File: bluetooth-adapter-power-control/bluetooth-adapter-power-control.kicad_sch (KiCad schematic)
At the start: 0 parts

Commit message: bluetooth-adapter-power-control: Finish schematic
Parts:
- added C1: 100n, symbol Device:C_Small
- added D1, D2: RED, symbol Device:LED
- added J1: UPDI, symbol Connector:Conn_01x03_Socket
- added J2: HDR, symbol Connector:Conn_01x05_Socket
- added Q1: NMOS, symbol Simulation_SPICE:NMOS
- added R1, R4: 10k, symbol Device:R
- added R2: 7.5k, symbol Device:R
- added R3, R5, R6: 1k, symbol Device:R
- added TP1: TestPoint, symbol Connector:TestPoint
- added U1: ATtiny202-SSNR, Package_SO:SOIC-8_3.9x4.9mm_P1.27mm, symbol MCU_Microchip_ATtiny:ATtiny202-SS
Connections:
- new net: Q1.2 (G), R3.2, R4.1
- new net: TP1.1, U1.2 (PA6)
- new net: R6.1, U1.3 (PA7)
- new net: D2.2 (A), R6.2
- new net: D1.2 (A), R5.2
- new net +5V: C1.1, J1.1 (Pin_1), J2.1 (Pin_1), R5.1, U1.1 (VCC)
- new net BTN1: Q1.1 (D)
- new net BTN2: Q1.3 (S)
- new net BTN_SHORT: J2.4 (Pin_4), R3.1, U1.5 (PA2)
- new net BT_LED_IN: J2.5 (Pin_5), U1.7 (PA3)
- new net CAR_ON: J2.3 (Pin_3), R1.2, R2.1, U1.4 (PA1)
- new net GND: C1.2, D1.1 (K), D2.1 (K), J1.3 (Pin_3), J2.2 (Pin_2), R2.2, R4.2, U1.8 (GND)
- new net IGNITION_IN: R1.1
- new net UPDI: J1.2 (Pin_2), U1.6 (~{RESET}/PA0)

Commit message: bluetooth-adapter-power-control: add footprints
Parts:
- C1: footprint (none) -> Capacitor_SMD:C_0603_1608Metric
- D1, D2: footprint (none) -> LED_SMD:LED_0603_1608Metric
- J1: footprint (none) -> Connector_PinHeader_1.27mm:PinHeader_1x05_P1.27mm_Vertical
- J2: footprint (none) -> Connector_PinHeader_1.27mm:PinHeader_1x03_P1.27mm_Vertical
- Q1: footprint (none) -> Package_TO_SOT_SMD:SOT-23
- R1, R2, R3, R4, R5, R6: footprint (none) -> Resistor_SMD:R_0603_1608Metric
- TP1: footprint (none) -> TestPoint:TestPoint_Pad_D1.0mm
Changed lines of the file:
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@@
 			)
 		)
-		(property "Footprint" ""
+		(property "Footprint" "Package_TO_SOT_SMD:SOT-23"
 			(at 60.96 101.6 0)
 			(effects
@@
 			)
 		)
-		(property "Footprint" ""
+		(property "Footprint" "Connector_PinHeader_1.27mm:PinHeader_1x05_P1.27mm_Vertical"
 			(at 50.8 149.86 0)
 			(effects
@@
 			)
 		)
-		(property "Footprint" ""
+		(property "Footprint" "TestPoint:TestPoint_Pad_D1.0mm"
 			(at 156.21 107.95 0)
 			(effects
@@
 			)
 		)
-		(property "Footprint" ""
+		(property "Footprint" "Resistor_SMD:R_0603_1608Metric"
 			(at 154.432 111.76 90)
 			(effects
@@
 			)
 		)
-		(property "Footprint" ""
+		(property "Footprint" "LED_SMD:LED_0603_1608Metric"
 			(at 193.04 106.68 0)
 			(effects
@@
 			)
 		)
-		(property "Footprint" ""
+		(property "Footprint" "Resistor_SMD:R_0603_1608Metric"
 			(at 38.862 110.49 90)
 			(effects
@@
 			)
 		)
-		(property "Footprint" ""
+		(property "Footprint" "Resistor_SMD:R_0603_1608Metric"
 			(at 38.862 97.79 90)
 			(effects
@@
 			)
 		)
-		(property "Footprint" ""
+		(property "Footprint" "Connector_PinHeader_1.27mm:PinHeader_1x03_P1.27mm_Vertical"
 			(at 250.19 105.41 0)
 			(effects
@@
 			)
 		)
-		(property "Footprint" ""
+		(property "Footprint" "LED_SMD:LED_0603_1608Metric"
 			(at 156.21 121.92 0)
 			(effects
@@
 			)
 		)
-		(property "Footprint" ""
+		(property "Footprint" "Resistor_SMD:R_0603_1608Metric"
 			(at 40.132 59.69 90)
 			(effects
@@
 			)
 		)
-		(property "Footprint" ""
+		(property "Footprint" "Resistor_SMD:R_0603_1608Metric"
 			(at 191.262 96.52 90)
 			(effects
@@
 			)
 		)
-		(property "Footprint" ""
+		(property "Footprint" "Resistor_SMD:R_0603_1608Metric"
 			(at 40.132 49.53 90)
 			(effects
@@
 			)
 		)
-		(property "Footprint" ""
+		(property "Footprint" "Capacitor_SMD:C_0603_1608Metric"
 			(at 93.98 100.33 0)
 			(effects

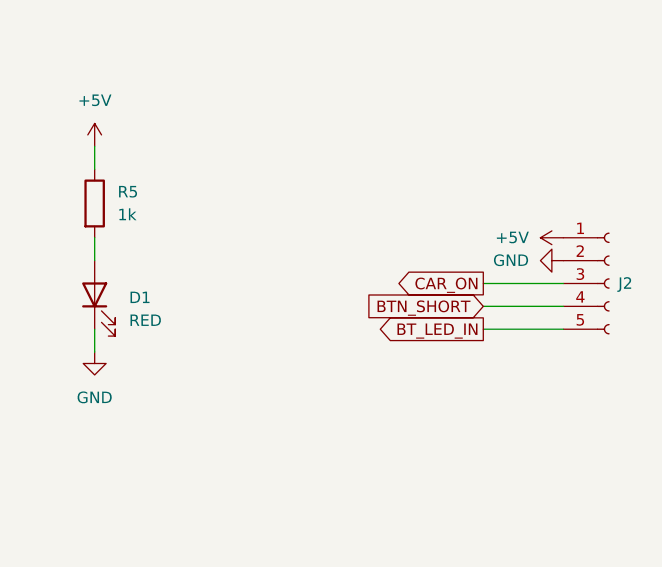
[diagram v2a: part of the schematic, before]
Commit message: bluetooth-adapter-power-control: Fix schematic & footprints, update PCB
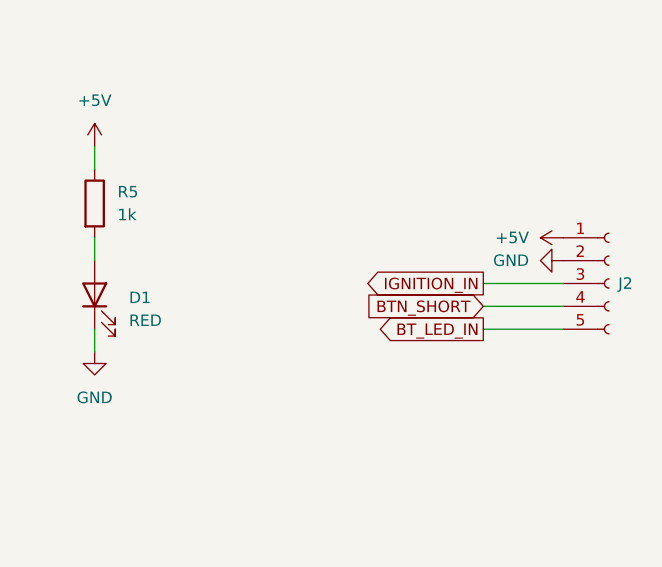
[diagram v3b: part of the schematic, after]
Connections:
- net CAR_ON: no longer J2.3 (Pin_3)
- net IGNITION_IN: now also J2.3 (Pin_3)
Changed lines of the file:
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@@
-		)
-	)
-	(global_label "CAR_ON"
-		(shape output)
-		(at 236.22 105.41 180)
-		(fields_autoplaced yes)
-		(effects
-			(font
-				(size 1.27 1.27)
-			)
-			(justify right)
-		)
-		(property "Intersheetrefs" "${INTERSHEET_REFS}"
-			(at 225.9776 105.41 0)
-			(effects
-				(font
-					(size 1.27 1.27)
-				)
-				(justify right)
-				(hide yes)
-			)
 		)
 	)
@@
 				(hide yes)
 			)
+		)
+	)
+	(global_label "IGNITION_IN"
+		(shape output)
+		(at 236.22 105.41 180)
+		(fields_autoplaced yes)
+		(effects
+			(font
+				(size 1.27 1.27)
+			)
+			(justify right)
+		)
+		(property "Intersheetrefs" "${INTERSHEET_REFS}"
+			(at 222.2884 105.41 0)
+			(effects
+				(font
+					(size 1.27 1.27)
+				)
+				(justify right)
+				(hide yes)
+			)

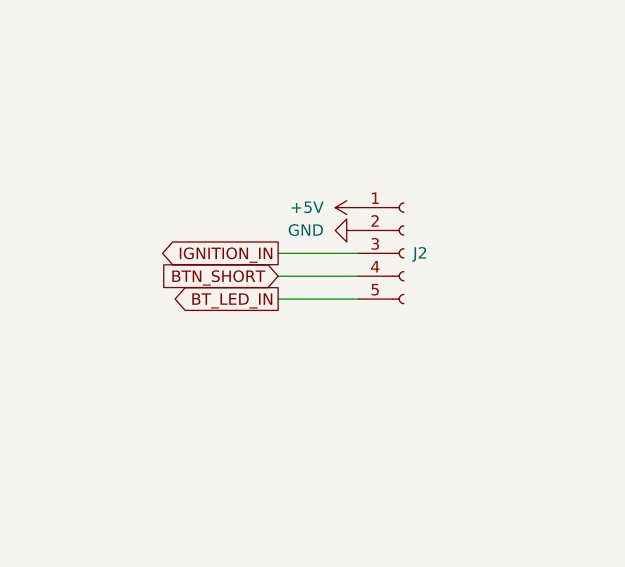
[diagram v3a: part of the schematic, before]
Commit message: bluetooth-adapter-power-control: change 5 pin header to 7 to include button short pins
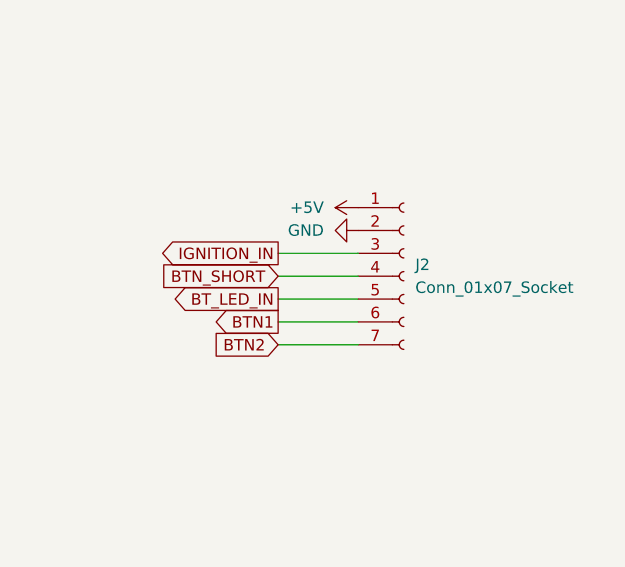
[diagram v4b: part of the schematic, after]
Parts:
- removed J2: HDR, Connector_PinHeader_1.27mm:PinHeader_1x03_P1.27mm_Vertical, symbol Connector:Conn_01x05_Socket
- added J2: Conn_01x07_Socket, Connector_PinHeader_1.27mm:PinHeader_1x07_P1.27mm_Vertical, symbol Connector:Conn_01x07_Socket
- J1: footprint Connector_PinHeader_1.27mm:PinHeader_1x05_P1.27mm_Vertical -> Connector_PinHeader_1.27mm:PinHeader_1x03_P1.27mm_Vertical
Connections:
- net +5V: now also J2.1 (Pin_1)
- net BTN1: now also J2.6 (Pin_6)
- net BTN2: now also J2.7 (Pin_7)
- net BTN_SHORT: now also J2.4 (Pin_4)
- net BT_LED_IN: now also J2.5 (Pin_5)
- net GND: now also J2.2 (Pin_2)
- net IGNITION_IN: now also J2.3 (Pin_3)
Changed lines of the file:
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@@
+	(wire
+		(pts
+			(xy 236.22 115.57) (xy 245.11 115.57)
+		)
+		(stroke
+			(width 0)
+			(type default)
+		)
+	)
+	(wire
+		(pts
+			(xy 236.22 113.03) (xy 245.11 113.03)
+		)
+		(stroke
+			(width 0)
+			(type default)
+		)
+	)
 	(wire
 		(pts
@@
 		)
 	)
+	(global_label "BTN2"
+		(shape input)
+		(at 236.22 115.57 180)
+		(fields_autoplaced yes)
+		(effects
+			(font
+				(size 1.27 1.27)
+			)
+			(justify right)
+		)
+		(property "Intersheetrefs" "${INTERSHEET_REFS}"
+			(at 228.4572 115.57 0)
+			(effects
+				(font
+					(size 1.27 1.27)
+				)
+				(justify right)
+				(hide yes)
+			)
+		)
+	)
 	(global_label "CAR_ON"
 		(shape input)
@@
 		(property "Intersheetrefs" "${INTERSHEET_REFS}"
 			(at 222.2884 105.41 0)
+			(effects
+				(font
+					(size 1.27 1.27)
+				)
+				(justify right)
+				(hide yes)
+			)
+		)
+	)
+	(global_label "BTN1"
+		(shape output)
+		(at 236.22 113.03 180)
+		(fields_autoplaced yes)
+		(effects
+			(font
+				(size 1.27 1.27)
+			)
+			(justify right)
+		)
+		(property "Intersheetrefs" "${INTERSHEET_REFS}"
+			(at 228.4572 113.03 0)
 			(effects
 				(font
@@
 			)
 		)
-		(property "Footprint" "Connector_PinHeader_1.27mm:PinHeader_1x05_P1.27mm_Vertical"
+		(property "Footprint" "Connector_PinHeader_1.27mm:PinHeader_1x03_P1.27mm_Vertical"
 			(at 50.8 149.86 0)
 			(effects
@@
 				(path "/cb952256-1cf9-427a-8657-67ac3ee7eb3e"
 					(reference "J1")
+					(unit 1)
+				)
+			)
+		)
+	)
+	(symbol
+		(lib_id "Connector:Conn_01x07_Socket")
+		(at 250.19 107.95 0)
+		(unit 1)
+		(exclude_from_sim no)
+		(in_bom yes)
+		(on_board yes)
+		(dnp no)
+		(fields_autoplaced yes)
+		(property "Reference" "J2"
+			(at 251.46 106.6799 0)
+			(effects
+				(font
+					(size 1.27 1.27)
+				)
+				(justify left)
+			)
+		)
+		(property "Value" "Conn_01x07_Socket"
+			(at 251.46 109.2199 0)
+			(effects
+				(font
+					(size 1.27 1.27)
+				)
+				(justify left)
+			)
+		)
+		(property "Footprint" "Connector_PinHeader_1.27mm:PinHeader_1x07_P1.27mm_Vertical"
+			(at 250.19 107.95 0)
+			(effects
+				(font
+					(size 1.27 1.27)
+				)
+				(hide yes)
+			)
+		)
+		(property "Datasheet" "~"
+			(at 250.19 107.95 0)
+			(effects
+				(font
+					(size 1.27 1.27)
+				)
+				(hide yes)
+			)
+		)
+		(property "Description" "Generic connector, single row, 01x07, script generated"
+			(at 250.19 107.95 0)
+			(effects
+				(font
+					(size 1.27 1.27)
+				)
+				(hide yes)
+			)
+		)
+		(pin "1"
+		)
+		(pin "6"
+		)
+		(pin "5"
+		)
+		(pin "2"
+		)
+		(pin "3"
+		)
+		(pin "4"
+		)
+		(pin "7"
+		)
+		(instances
+			(project ""
+				(path "/cb952256-1cf9-427a-8657-67ac3ee7eb3e"
+					(reference "J2")
 					(unit 1)
 				)
@@
 					(unit 1)
 				)
-			)
-		)
-	)
-	(symbol
-		(lib_id "Connector:Conn_01x05_Socket")
-		(at 250.19 105.41 0)
-		(unit 1)
-		(exclude_from_sim no)
-		(in_bom yes)
-		(on_board yes)
-		(dnp no)
-		(property "Reference" "J2"
-			(at 251.206 105.41 0)
-			(effects
-				(font
-					(size 1.27 1.27)
-				)
-				(justify left)
-			)
-		)
-		(property "Value" "HDR"
-			(at 251.46 106.6799 0)
-			(effects
-				(font
-					(size 1.27 1.27)
-				)
-				(justify left)
-				(hide yes)
-			)
-		)
-		(property "Footprint" "Connector_PinHeader_1.27mm:PinHeader_1x03_P1.27mm_Vertical"
-			(at 250.19 105.41 0)
-			(effects
-				(font
-					(size 1.27 1.27)
-				)
-				(hide yes)
-			)
-		)
-		(property "Datasheet" "~"
-			(at 250.19 105.41 0)
-			(effects
-				(font
-					(size 1.27 1.27)
-				)
-				(hide yes)
-			)
-		)
-		(property "Description" "Generic connector, single row, 01x05, script generated"
-			(at 250.19 105.41 0)
-			(effects
-				(font
-					(size 1.27 1.27)
-				)
-				(hide yes)
-			)
-		)
-		(pin "1"
-		)
-		(pin "2"
-		)
-		(pin "3"
-		)
-		(pin "4"
-		)
-		(pin "5"
-		)
-		(instances
-			(project ""
-				(path "/cb952256-1cf9-427a-8657-67ac3ee7eb3e"
-					(reference "J2")
-					(unit 1)
-				)

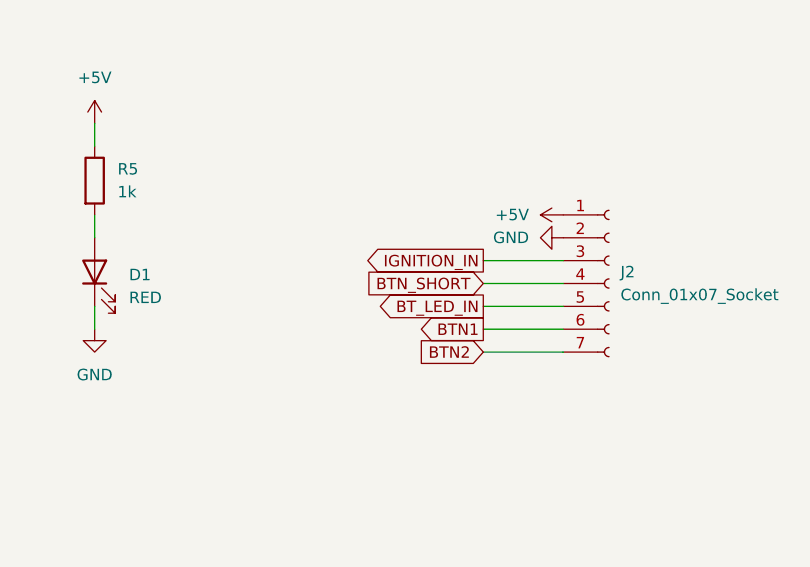
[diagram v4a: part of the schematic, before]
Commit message: bluetooth-adapter-power-control: Finish PCB routing
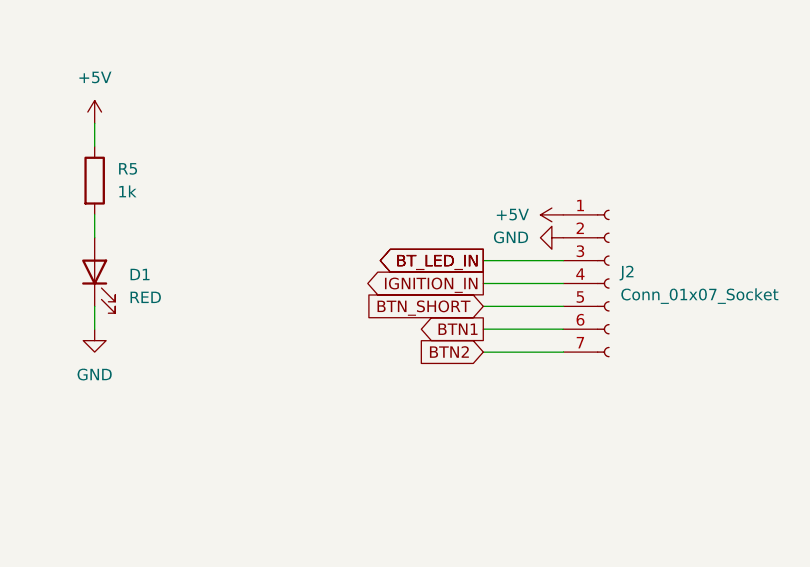
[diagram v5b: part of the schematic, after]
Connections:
- net BTN_SHORT: now also J2.5 (Pin_5); no longer J2.4 (Pin_4)
- net BT_LED_IN: now also J2.3 (Pin_3); no longer J2.5 (Pin_5)
- net IGNITION_IN: now also J2.4 (Pin_4); no longer J2.3 (Pin_3)
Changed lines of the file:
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@@
 		)
 	)
-	(global_label "BTN_SHORT"
-		(shape input)
+	(global_label "IGNITION_IN"
+		(shape output)
 		(at 236.22 107.95 180)
 		(fields_autoplaced yes)
@@
 		)
 		(property "Intersheetrefs" "${INTERSHEET_REFS}"
-			(at 222.591 107.95 0)
-			(effects
-				(font
-					(size 1.27 1.27)
-				)
-				(justify right)
-				(hide yes)
-			)
-		)
-	)
-	(global_label "BT_LED_IN"
-		(shape output)
-		(at 236.22 110.49 180)
-		(fields_autoplaced yes)
-		(effects
-			(font
-				(size 1.27 1.27)
-			)
-			(justify right)
-		)
-		(property "Intersheetrefs" "${INTERSHEET_REFS}"
-			(at 223.6796 110.49 0)
+			(at 222.2884 107.95 0)
 			(effects
 				(font
@@
 		)
 	)
-	(global_label "IGNITION_IN"
+	(global_label "BT_LED_IN"
 		(shape output)
 		(at 236.22 105.41 180)
@@
 		)
 		(property "Intersheetrefs" "${INTERSHEET_REFS}"
-			(at 222.2884 105.41 0)
+			(at 223.6796 105.41 0)
 			(effects
 				(font
@@
 			(effects
 				(font
+					(size 1.27 1.27)
+				)
+				(justify right)
+				(hide yes)
+			)
+		)
+	)
+	(global_label "BTN_SHORT"
+		(shape input)
+		(at 236.22 110.49 180)
+		(fields_autoplaced yes)
+		(effects
+			(font
+				(size 1.27 1.27)
+			)
+			(justify right)
+		)
+		(property "Intersheetrefs" "${INTERSHEET_REFS}"
+			(at 222.591 110.49 0)
+			(effects
+				(font
+					(size 1.27 1.27)
+				)
+				(justify right)
+				(hide yes)
+			)
+		)
+	)
+	(global_label "BT_LED_IN"
+		(shape output)
+		(at 236.22 105.41 180)
+		(fields_autoplaced yes)
+		(effects
+			(font
+				(size 1.27 1.27)
+			)
+			(justify right)
+		)
+		(property "Intersheetrefs" "${INTERSHEET_REFS}"
+			(at 223.6796 105.41 0)
+			(effects
+				(font
